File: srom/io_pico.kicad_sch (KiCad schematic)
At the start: 5 parts, among them J201 Conn_01x03_Female, J202 Conn_01x06_Female, U201 Pico-2 IO, U202 APS6404L-3SQR_PSRAM64Mbit

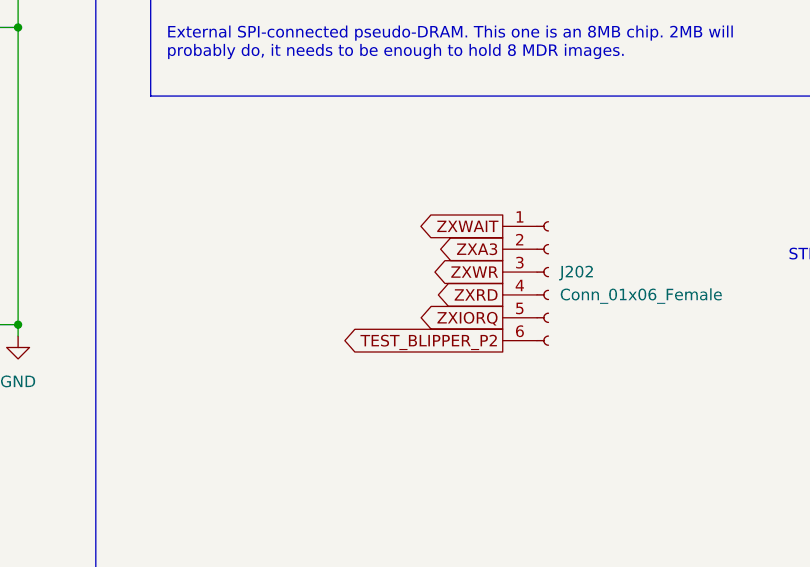
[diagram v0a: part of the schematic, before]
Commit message: add SD card detect to hardware
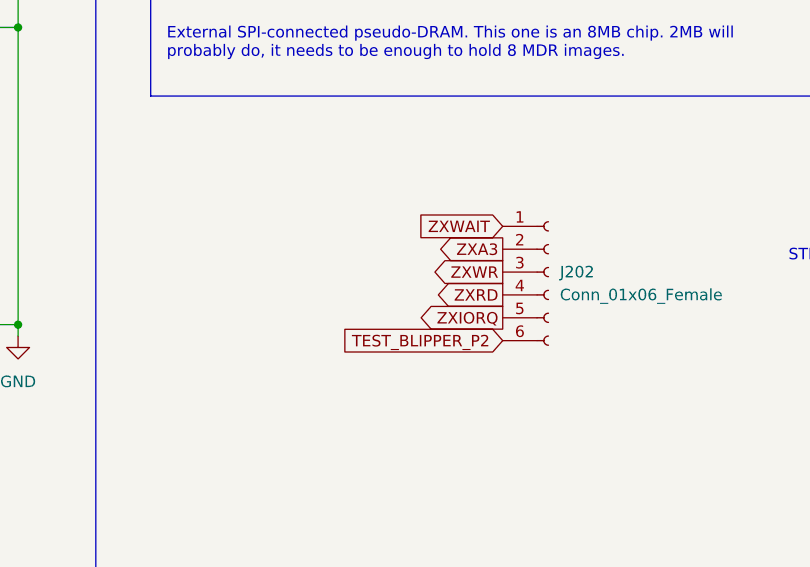
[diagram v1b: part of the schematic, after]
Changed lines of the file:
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@@
     )
   )
-  (global_label "ZXWAIT" (shape output) (at 175.26 96.266 180) (fields_autoplaced)
+  (global_label "ZXWAIT" (shape input) (at 175.26 96.266 180) (fields_autoplaced)
     (effects (font (size 1.27 1.27)) (justify right))
     (property "Intersheet References" "${INTERSHEET_REFS}" (id 0) (at 166.3155 96.1866 0)
@@
     )
   )
-  (global_label "TEST_BLIPPER_P2" (shape output) (at 175.26 108.966 180) (fields_autoplaced)
+  (global_label "TEST_BLIPPER_P2" (shape input) (at 175.26 108.966 180) (fields_autoplaced)
     (effects (font (size 1.27 1.27)) (justify right))
     (property "Intersheet References" "${INTERSHEET_REFS}" (id 0) (at 156.2764 108.8866 0)

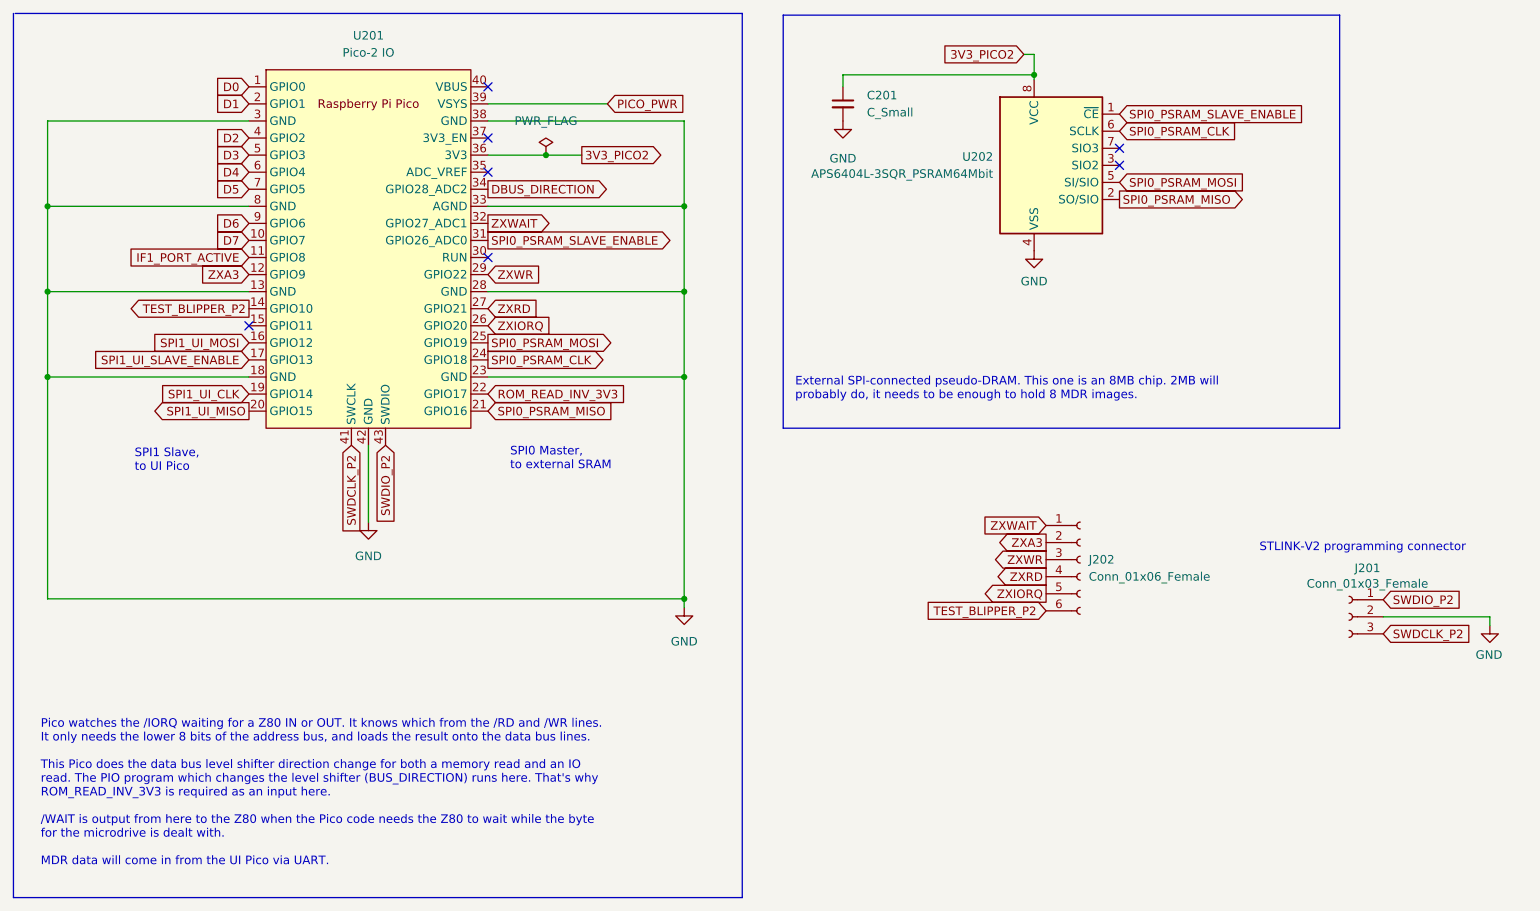
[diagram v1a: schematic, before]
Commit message: update schematic to match UART comms and SD card detect
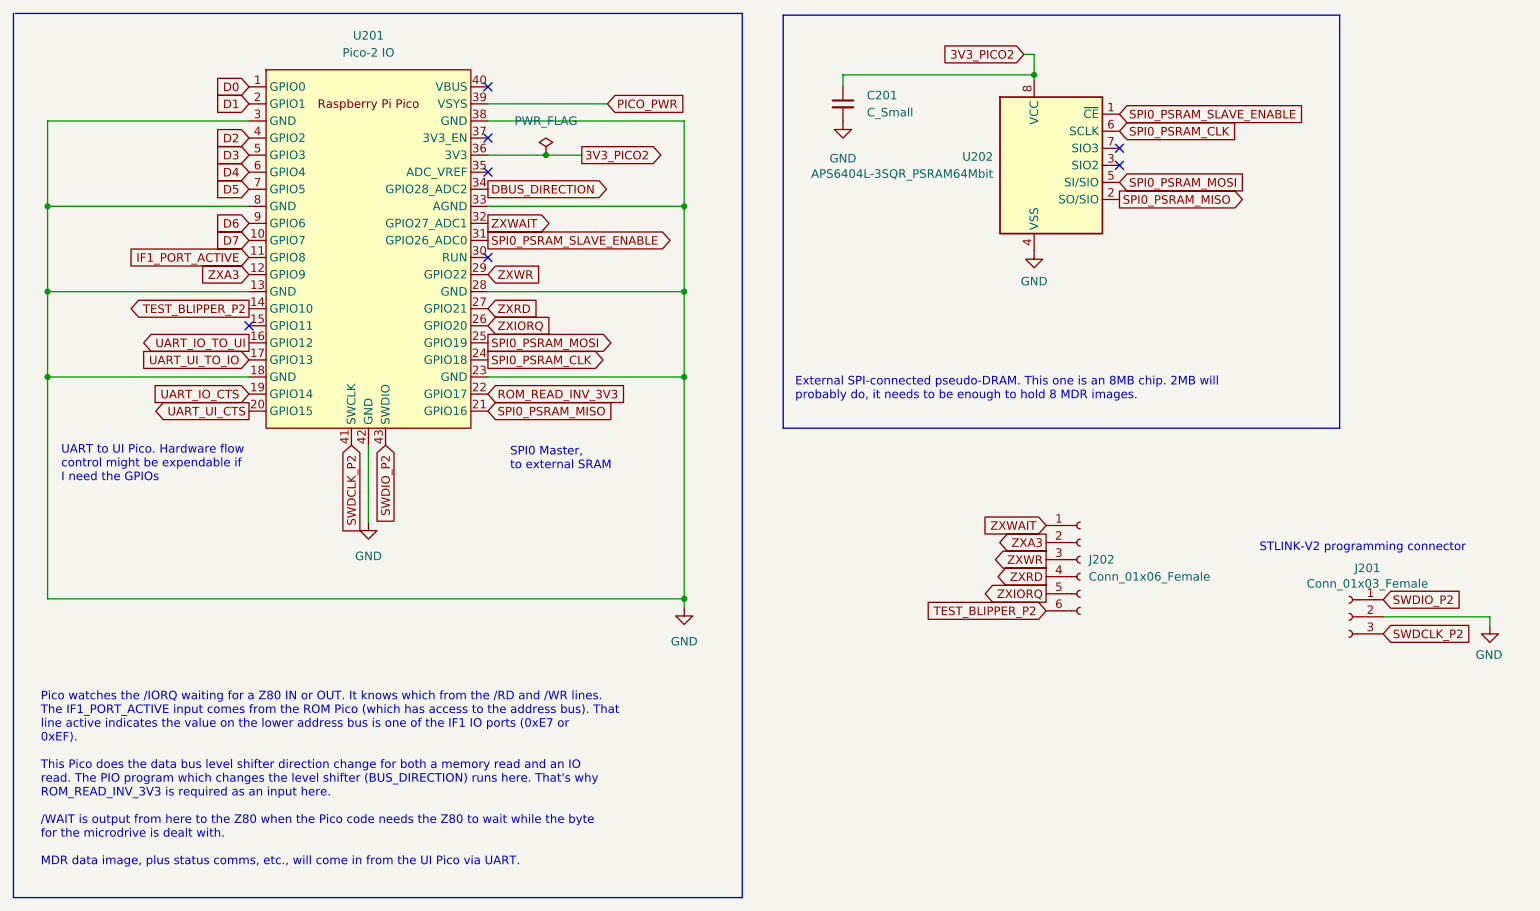
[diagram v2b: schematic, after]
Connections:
- net SPI1_UI_CLK renamed UART_IO_CTS
- net SPI1_UI_MISO renamed UART_UI_CTS
- net SPI1_UI_MOSI renamed UART_IO_TO_UI
- net SPI1_UI_SLAVE_ENABLE renamed UART_UI_TO_IO
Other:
- note added: "Pico watches the /IORQ waiting for a Z80 IN or OUT. It knows which from the /RD and /WR lines. The IF1_PORT_ACTIVE input comes from the ROM Pico (which has access to the address bus). That line active indicates the value on the lower address bus is one of the IF1 IO ports (0xE7 or 0xEF). This Pico does the data bus level shifter direction change for both a memory read and an IO read. The PIO prog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"
- note added: "UART to UI Pico. Hardware flow control might be expendable if I need the GPIOs"
- note removed: "Pico watches the /IORQ waiting for a Z80 IN or OUT. It knows which from the /RD and /WR lines. It only needs the lower 8 bits of the address bus, and loads the result onto the data bus lines. This Pico does the data bus level shifter direction change for both a memory read and an IO read. The PIO program which changes the level shifter (BUS_DIRECTION) runs here. That's why ROM_READ_INV_3V3 is req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"
- note removed: "SPI1 Slave, to UI Pico"
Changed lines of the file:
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@@
     (effects (font (size 1.27 1.27)) (justify left bottom))
   )
-  (text "Pico watches the /IORQ waiting for a Z80 IN or OUT. It knows which from the /RD and /WR lines.\nIt only needs the lower 8 bits of the address bus, and loads the result onto the data bus lines.\n\nThis Pico does the data bus level shifter direction change for both a memory read and an IO\nread. The PIO program which changes the level shifter (BUS_DIRECTION) runs here. That's why\nROM_READ_INV_3V3 is required as an input here.\n\n/WAIT is output from here to the Z80 when the Pico code needs the Z80 to wait while the byte\nfor the microdrive is dealt with.\n\nMDR data will come in from the UI Pico via UART.\n"
+  (text "Pico watches the /IORQ waiting for a Z80 IN or OUT. It knows which from the /RD and /WR lines.\nThe IF1_PORT_ACTIVE input comes from the ROM Pico (which has access to the address bus). That\nline active indicates the value on the lower address bus is one of the IF1 IO ports (0xE7 or\n0xEF).\n\nThis Pico does the data bus level shifter direction change for both a memory read and an IO\nread. The PIO program which changes the level shifter (BUS_DIRECTION) runs here. That's why\nROM_READ_INV_3V3 is required as an input here.\n\n/WAIT is output from here to the Z80 when the Pico code needs the Z80 to wait while the byte\nfor the microdrive is dealt with.\n\nMDR data image, plus status comms, etc., will come in from the UI Pico via UART.\n"
     (at 25.654 147.066 0)
     (effects (font (size 1.27 1.27)) (justify left bottom))
@@
     (effects (font (size 1.27 1.27)) (justify left bottom))
   )
-  (text "SPI1 Slave,\nto UI Pico" (at 39.624 88.392 0)
+  (text "UART to UI Pico. Hardware flow\ncontrol might be expendable if\nI need the GPIOs"
+    (at 28.702 89.916 0)
     (effects (font (size 1.27 1.27)) (justify left bottom))
   )
@@
     )
   )
-  (global_label "SPI1_UI_MISO" (shape output) (at 56.642 79.248 180) (fields_autoplaced)
-    (effects (font (size 1.27 1.27)) (justify right))
-    (property "Intersheet References" "${INTERSHEET_REFS}" (id 0) (at 41.4684 79.1686 0)
+  (global_label "UART_IO_CTS" (shape input) (at 56.642 76.708 180) (fields_autoplaced)
+    (effects (font (size 1.27 1.27)) (justify right))
+    (property "Intersheet References" "${INTERSHEET_REFS}" (id 0) (at 42.2546 76.6286 0)
       (effects (font (size 1.27 1.27)) (justify right) hide)
     )
@@
     )
   )
-  (global_label "SPI1_UI_SLAVE_ENABLE" (shape input) (at 56.642 71.628 180) (fields_autoplaced)
-    (effects (font (size 1.27 1.27)) (justify right))
-    (property "Intersheet References" "${INTERSHEET_REFS}" (id 0) (at 32.5179 71.5486 0)
+  (global_label "UART_UI_TO_IO" (shape input) (at 56.642 71.628 180) (fields_autoplaced)
+    (effects (font (size 1.27 1.27)) (justify right))
+    (property "Intersheet References" "${INTERSHEET_REFS}" (id 0) (at 40.5008 71.5486 0)
       (effects (font (size 1.27 1.27)) (justify right) hide)
     )
@@
     )
   )
-  (global_label "SPI1_UI_MOSI" (shape input) (at 56.642 69.088 180) (fields_autoplaced)
-    (effects (font (size 1.27 1.27)) (justify right))
-    (property "Intersheet References" "${INTERSHEET_REFS}" (id 0) (at 41.4684 69.0086 0)
+  (global_label "UART_IO_TO_UI" (shape output) (at 56.642 69.088 180) (fields_autoplaced)
+    (effects (font (size 1.27 1.27)) (justify right))
+    (property "Intersheet References" "${INTERSHEET_REFS}" (id 0) (at 40.5008 69.0086 0)
       (effects (font (size 1.27 1.27)) (justify right) hide)
     )
@@
     )
   )
-  (global_label "SPI1_UI_CLK" (shape input) (at 56.642 76.708 180) (fields_autoplaced)
-    (effects (font (size 1.27 1.27)) (justify right))
-    (property "Intersheet References" "${INTERSHEET_REFS}" (id 0) (at 42.4965 76.6286 0)
-      (effects (font (size 1.27 1.27)) (justify right) hide)
-    )
+  (global_label "UART_UI_CTS" (shape output) (at 56.642 79.248 180) (fields_autoplaced)
+    (effects (font (size 1.27 1.27)) (justify right))
+    (property "Intersheet References" "${INTERSHEET_REFS}" (id 0) (at 42.2546 79.1686 0)
+      (effects (font (size 1.27 1.27)) (justify right) hide)
+    )

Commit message: add some LEDs to schematic
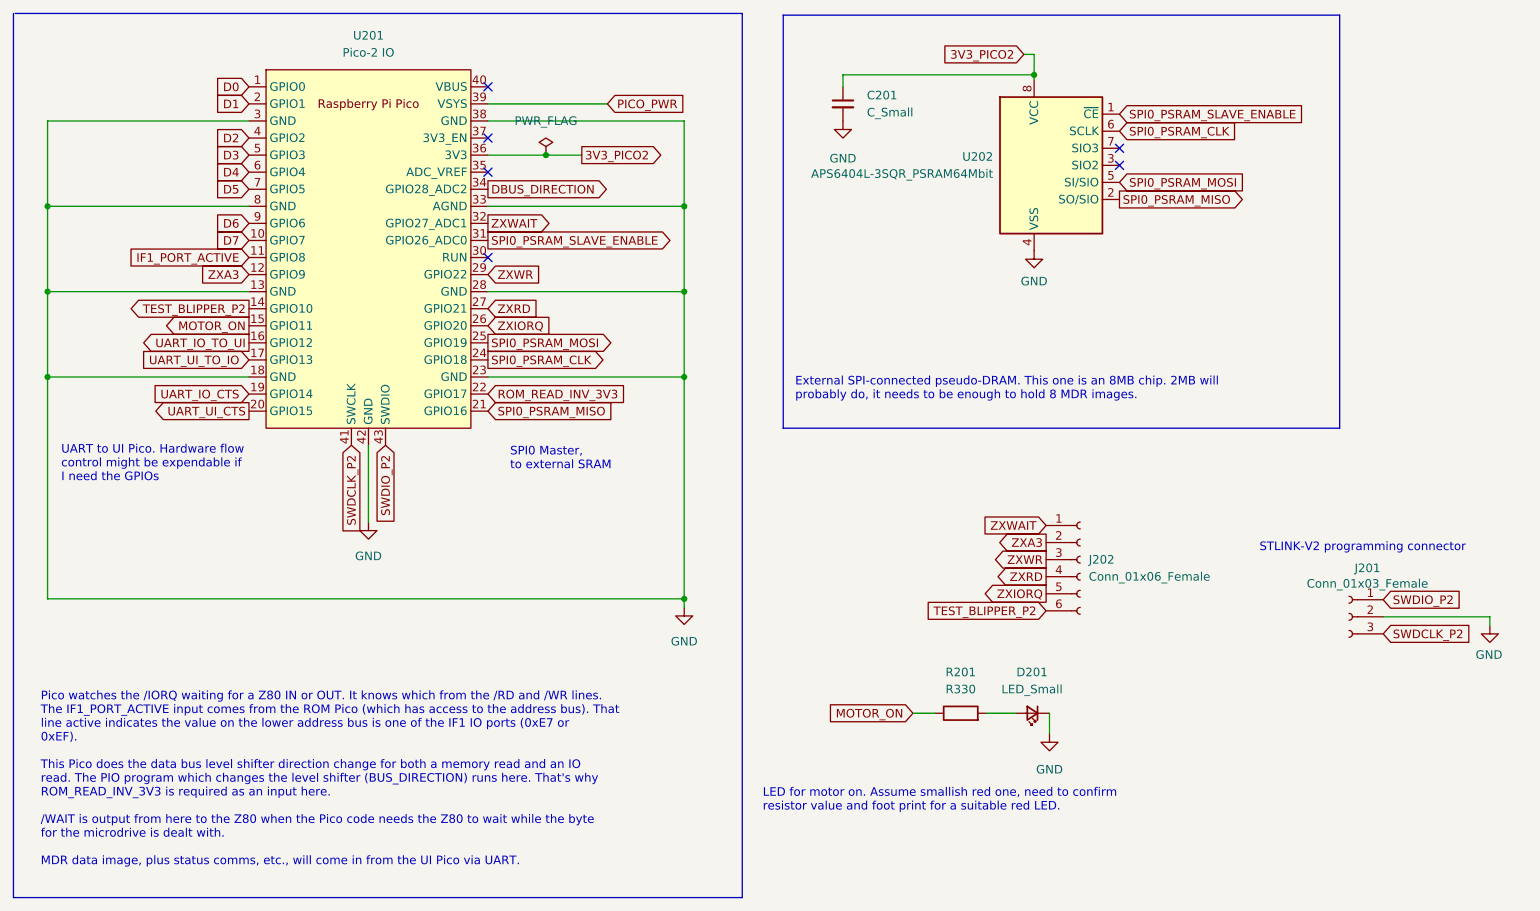
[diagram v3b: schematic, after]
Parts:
- added D201: LED_Small, LED_THT:LED_D3.0mm, symbol Device:LED_Small
- added R201: R330, Resistor_SMD:R_1206_3216Metric_Pad1.30x1.75mm_HandSolder, symbol Device:R
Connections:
- net GND: now also D201.1 (K)
- net MOTOR_ON: now reaches U201.15 (GPIO11)
- net MOTOR_ON: now also R201.1
- new net: D201.2 (A), R201.2
- no-connect marks 7 -> 6
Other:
- note added: "LED for motor on. Assume smallish red one, need to confirm resistor value and foot print for a suitable red LED."
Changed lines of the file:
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@@
   (no_connect (at 92.202 38.608))
   (no_connect (at 186.182 40.132))
-  (no_connect (at 56.642 66.548))
   (no_connect (at 92.202 56.388))
+  (wire (pts (xy 166.37 124.206) (xy 170.688 124.206))
+    (stroke (width 0) (type default) (color 0 0 0 0))
+  )
   (wire (pts (xy 26.67 61.468) (xy 56.642 61.468))
     (stroke (width 0) (type default) (color 0 0 0 0))
@@
     (stroke (width 0) (type default) (color 0 0 0 0))
   )
+  (wire (pts (xy 175.768 127.254) (xy 175.768 124.206))
+    (stroke (width 0) (type default) (color 0 0 0 0))
+  )
   (polyline (pts (xy 218.948 20.32) (xy 218.948 81.788))
     (stroke (width 0) (type default) (color 0 0 0 0))
@@
   )
   (wire (pts (xy 100.838 41.148) (xy 106.172 41.148))
+    (stroke (width 0) (type default) (color 0 0 0 0))
+  )
+  (wire (pts (xy 155.448 124.206) (xy 158.75 124.206))
     (stroke (width 0) (type default) (color 0 0 0 0))
   )
@@
     (effects (font (size 1.27 1.27)) (justify left bottom))
   )
+  (text "LED for motor on. Assume smallish red one, need to confirm\nresistor value and foot print for a suitable red LED."
+    (at 133.096 138.938 0)
+    (effects (font (size 1.27 1.27)) (justify left bottom))
+  )
   (global_label "ZXIORQ" (shape output) (at 175.26 106.426 180) (fields_autoplaced)
     (effects (font (size 1.27 1.27)) (justify right))
@@
     )
   )
+  (global_label "MOTOR_ON" (shape output) (at 56.642 66.548 180) (fields_autoplaced)
+    (effects (font (size 1.27 1.27)) (justify right))
+    (property "Intersheet References" "${INTERSHEET_REFS}" (id 0) (at 44.2503 66.4686 0)
+      (effects (font (size 1.27 1.27)) (justify right) hide)
+    )
+  )
   (global_label "3V3_PICO2" (shape input) (at 171.958 26.162 180) (fields_autoplaced)
     (effects (font (size 1.27 1.27)) (justify right))
@@
     )
   )
+  (global_label "MOTOR_ON" (shape input) (at 155.448 124.206 180) (fields_autoplaced)
+    (effects (font (size 1.27 1.27)) (justify right))
+    (property "Intersheet References" "${INTERSHEET_REFS}" (id 0) (at 143.0563 124.1266 0)
+      (effects (font (size 1.27 1.27)) (justify right) hide)
+    )
+  )
   (global_label "ZXRD" (shape input) (at 92.202 64.008 0) (fields_autoplaced)
     (effects (font (size 1.27 1.27)) (justify left))
@@
       (effects (font (size 1.27 1.27)) (justify right) hide)
     )
+  )
+  (symbol (lib_id "power:GND") (at 175.768 127.254 0) (unit 1)
+    (in_bom yes) (on_board yes) (fields_autoplaced)
+    (property "Reference" "#PWR0106" (id 0) (at 175.768 133.604 0)
+      (effects (font (size 1.27 1.27)) hide)
+    )
+    (property "Value" "GND" (id 1) (at 175.768 132.588 0))
+    (property "Footprint" "" (id 2) (at 175.768 127.254 0)
+      (effects (font (size 1.27 1.27)) hide)
+    )
+    (property "Datasheet" "" (id 3) (at 175.768 127.254 0)
+      (effects (font (size 1.27 1.27)) hide)
+    )
+    (pin "1")
   )
   (symbol (lib_id "power:PWR_FLAG") (at 100.838 41.148 0) (unit 1)
@@
     )
     (pin "1")
+  )
+  (symbol (lib_id "Device:LED_Small") (at 173.228 124.206 180) (unit 1)
+    (in_bom yes) (on_board yes) (fields_autoplaced)
+    (property "Reference" "D201" (id 0) (at 173.1645 118.11 0))
+    (property "Value" "LED_Small" (id 1) (at 173.1645 120.65 0))
+    (property "Footprint" "LED_THT:LED_D3.0mm" (id 2) (at 173.228 124.206 90)
+      (effects (font (size 1.27 1.27)) hide)
+    )
+    (property "Datasheet" "~" (id 3) (at 173.228 124.206 90)
+      (effects (font (size 1.27 1.27)) hide)
+    )
+    (pin "1")
+    (pin "2")
   )
   (symbol (lib_id "Connector:Conn_01x03_Female") (at 220.345 109.855 0) (mirror y) (unit 1)
@@
     (pin "1")
   )
+  (symbol (lib_id "Device:R") (at 162.56 124.206 90) (unit 1)
+    (in_bom yes) (on_board yes) (fields_autoplaced)
+    (property "Reference" "R201" (id 0) (at 162.56 118.11 90))
+    (property "Value" "R330" (id 1) (at 162.56 120.65 90))
+    (property "Footprint" "Resistor_SMD:R_1206_3216Metric_Pad1.30x1.75mm_HandSolder" (id 2) (at 162.56 125.984 90)
+      (effects (font (size 1.27 1.27)) hide)
+    )
+    (property "Datasheet" "~" (id 3) (at 162.56 124.206 0)
+      (effects (font (size 1.27 1.27)) hide)
+    )
+    (pin "1")
+    (pin "2")
+  )
   (symbol (lib_id "Connector:Conn_01x06_Female") (at 180.34 101.346 0) (unit 1)
